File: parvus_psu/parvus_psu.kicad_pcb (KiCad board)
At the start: 2 copper layers, 70 x 100 mm, 30 parts, among them J1 tr_sec, J2 switch, J3 ac_input, J4 tr_pri, J5 left_power, J6 right_power

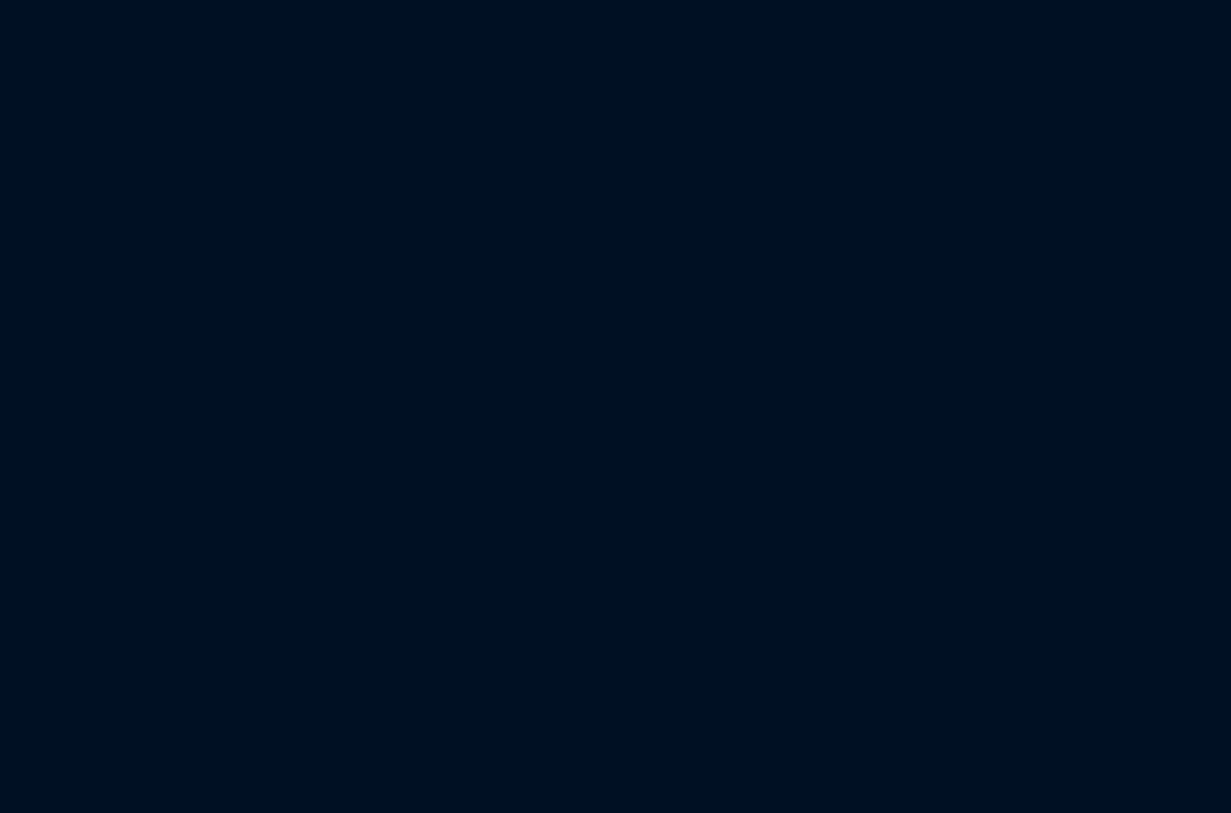
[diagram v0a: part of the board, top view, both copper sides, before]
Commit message: Finished schematic for AC detection circuit and clipping signaling.
Signed-off-by: Nenad Radulovic <nenad.b.radulovic@gmail.com>
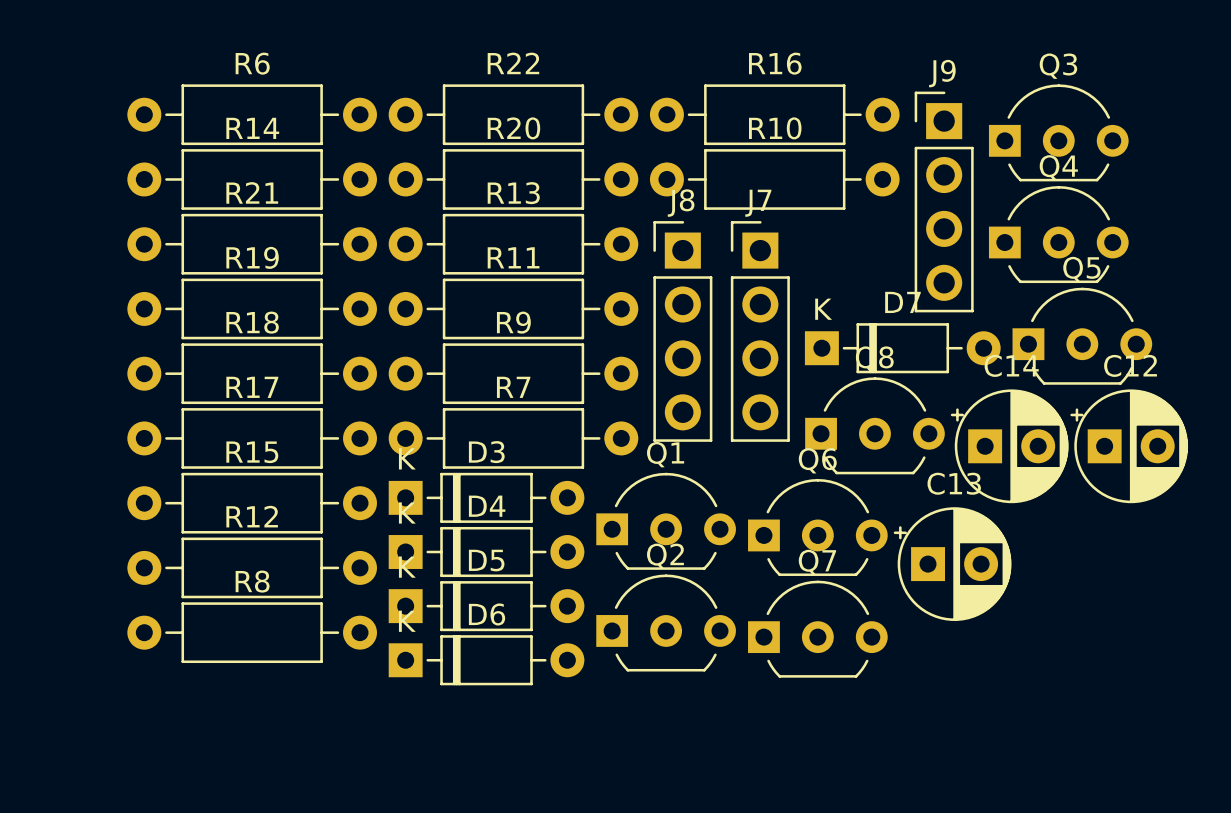
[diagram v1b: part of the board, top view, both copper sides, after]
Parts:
- added C12: 1u, Capacitor_THT:CP_Radial_D5.0mm_P2.50mm, F.Cu at (186.4, 57.1)
- added C13: 1u, Capacitor_THT:CP_Radial_D5.0mm_P2.50mm, F.Cu at (178.0, 62.6)
- added C14: 1u, Capacitor_THT:CP_Radial_D5.0mm_P2.50mm, F.Cu at (180.7, 57.1)
- added D3: 1N4148, Diode_THT:D_DO-35_SOD27_P7.62mm_Horizontal, F.Cu at (153.4, 59.5)
- added D4: 1N4148, Diode_THT:D_DO-35_SOD27_P7.62mm_Horizontal, F.Cu at (153.4, 62.1)
- added D5: 1N4148, Diode_THT:D_DO-35_SOD27_P7.62mm_Horizontal, F.Cu at (153.4, 64.6)
- added D6: 1N4148, Diode_THT:D_DO-35_SOD27_P7.62mm_Horizontal, F.Cu at (153.4, 67.2)
- added D7: 1N4148, Diode_THT:D_DO-35_SOD27_P7.62mm_Horizontal, F.Cu at (173.0, 52.5)
- added J7: signal, Connector_PinHeader_2.54mm:PinHeader_1x04_P2.54mm_Vertical, F.Cu at (170.1, 47.9)
- added J8: ctrl_1, Connector_PinHeader_2.54mm:PinHeader_1x04_P2.54mm_Vertical, F.Cu at (166.5, 47.9)
- added J9: ctrl_2, Connector_PinHeader_2.54mm:PinHeader_1x04_P2.54mm_Vertical, F.Cu at (178.8, 41.8)
- added Q1: BC546B, Package_TO_SOT_THT:TO-92_Inline_Wide, F.Cu at (163.2, 61.0)
- added Q2: BC546B, Package_TO_SOT_THT:TO-92_Inline_Wide, F.Cu at (163.2, 65.8)
- added Q3: BC546B, Package_TO_SOT_THT:TO-92_Inline_Wide, F.Cu at (181.7, 42.7)
- added Q4: BC546B, Package_TO_SOT_THT:TO-92_Inline_Wide, F.Cu at (181.7, 47.5)
- added Q5: BC546B, Package_TO_SOT_THT:TO-92_Inline_Wide, F.Cu at (182.8, 52.3)
- added Q6: BC556B, Package_TO_SOT_THT:TO-92_Inline_Wide, F.Cu at (170.3, 61.3)
- added Q7: BC556B, Package_TO_SOT_THT:TO-92_Inline_Wide, F.Cu at (170.3, 66.1)
- added Q8: BC556B, Package_TO_SOT_THT:TO-92_Inline_Wide, F.Cu at (173.0, 56.5)
- added R10: 100k, Resistor_THT:R_Axial_DIN0207_L6.3mm_D2.5mm_P10.16mm_Horizontal, F.Cu at (165.7, 44.5)
- added R11: 100, Resistor_THT:R_Axial_DIN0207_L6.3mm_D2.5mm_P10.16mm_Horizontal, F.Cu at (153.4, 50.6)
- added R12: 100k, Resistor_THT:R_Axial_DIN0207_L6.3mm_D2.5mm_P10.16mm_Horizontal, F.Cu at (141.1, 62.8)
- added R13: 100, Resistor_THT:R_Axial_DIN0207_L6.3mm_D2.5mm_P10.16mm_Horizontal, F.Cu at (153.4, 47.6)
- added R14: 100k, Resistor_THT:R_Axial_DIN0207_L6.3mm_D2.5mm_P10.16mm_Horizontal, F.Cu at (141.1, 44.5)
- added R15: 100k, Resistor_THT:R_Axial_DIN0207_L6.3mm_D2.5mm_P10.16mm_Horizontal, F.Cu at (141.1, 59.8)
- added R16: 22k, Resistor_THT:R_Axial_DIN0207_L6.3mm_D2.5mm_P10.16mm_Horizontal, F.Cu at (165.7, 41.5)
- added R17: 22k, Resistor_THT:R_Axial_DIN0207_L6.3mm_D2.5mm_P10.16mm_Horizontal, F.Cu at (141.1, 56.7)
- added R18: 22k, Resistor_THT:R_Axial_DIN0207_L6.3mm_D2.5mm_P10.16mm_Horizontal, F.Cu at (141.1, 53.7)
- added R19: 22k, Resistor_THT:R_Axial_DIN0207_L6.3mm_D2.5mm_P10.16mm_Horizontal, F.Cu at (141.1, 50.6)
- added R20: 22k, Resistor_THT:R_Axial_DIN0207_L6.3mm_D2.5mm_P10.16mm_Horizontal, F.Cu at (153.4, 44.5)
- added R21: 10k, Resistor_THT:R_Axial_DIN0207_L6.3mm_D2.5mm_P10.16mm_Horizontal, F.Cu at (141.1, 47.6)
- added R22: 10k, Resistor_THT:R_Axial_DIN0207_L6.3mm_D2.5mm_P10.16mm_Horizontal, F.Cu at (153.4, 41.5)
- added R6: 100k, Resistor_THT:R_Axial_DIN0207_L6.3mm_D2.5mm_P10.16mm_Horizontal, F.Cu at (141.1, 41.5)
- added R7: 10k, Resistor_THT:R_Axial_DIN0207_L6.3mm_D2.5mm_P10.16mm_Horizontal, F.Cu at (153.4, 56.7)
- added R8: 47k, Resistor_THT:R_Axial_DIN0207_L6.3mm_D2.5mm_P10.16mm_Horizontal, F.Cu at (141.1, 65.9)
- added R9: 100k, Resistor_THT:R_Axial_DIN0207_L6.3mm_D2.5mm_P10.16mm_Horizontal, F.Cu at (153.4, 53.7)
- J5: value left_power -> power_1
- J6: value right_power -> power_2
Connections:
- net /acs_n renamed acs_n
- net /acs_p renamed acs_p

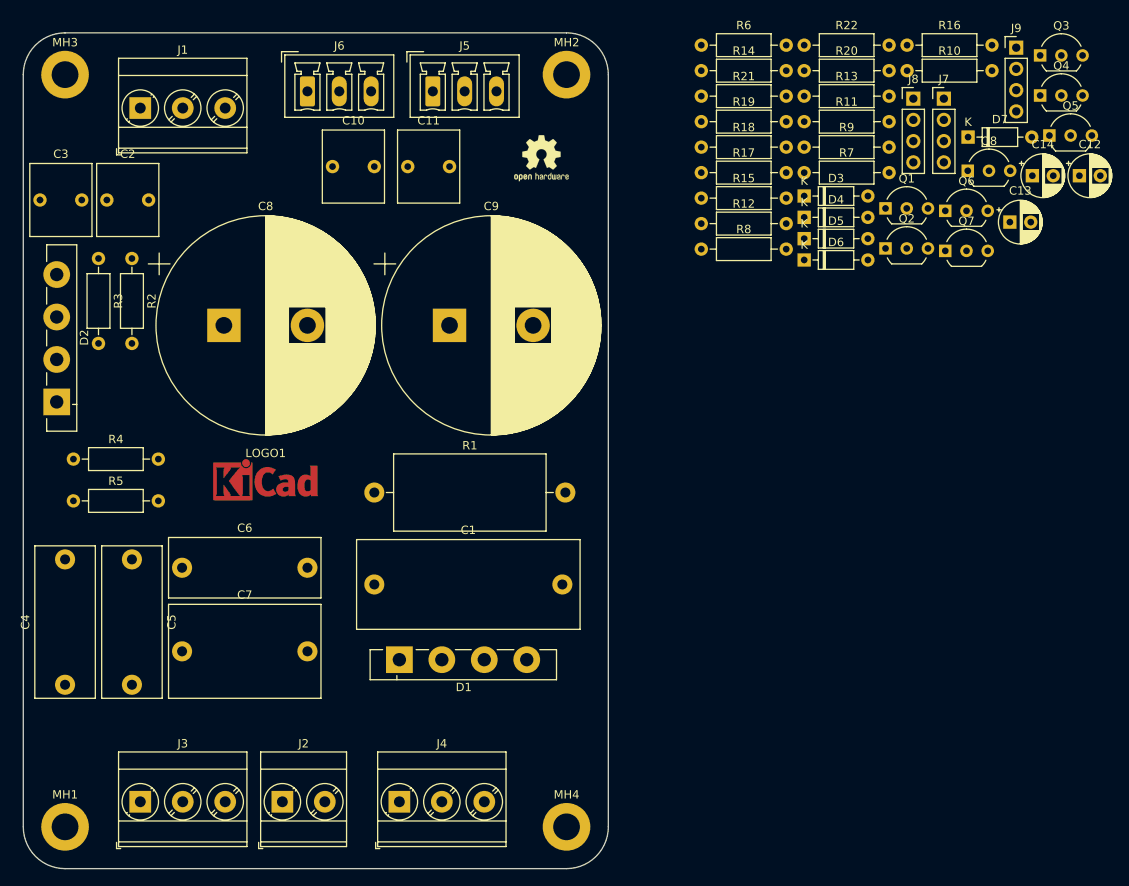
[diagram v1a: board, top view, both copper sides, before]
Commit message: Preliminary placement of AC detect and clipping circuitry.
Signed-off-by: Nenad Radulovic <nenad.b.radulovic@gmail.com>
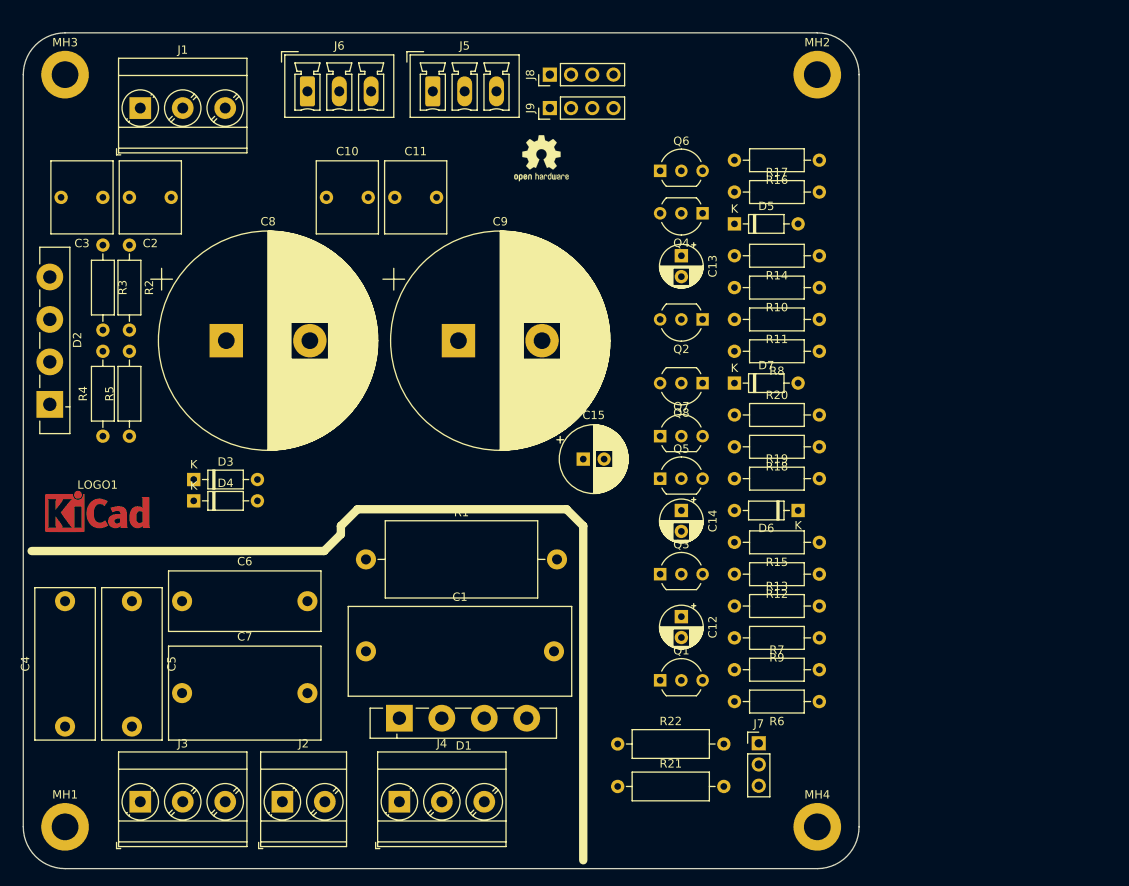
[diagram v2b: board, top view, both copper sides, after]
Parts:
- added C15: 10u, Capacitor_THT:CP_Radial_D8.0mm_P2.50mm, F.Cu at (127.0, 91.0)
- C12, C14: value 1u -> 2u2
- C13: value 1u -> 4u7
- J7: footprint Connector_PinHeader_2.54mm:PinHeader_1x04_P2.54mm_Vertical -> Connector_PinHeader_2.54mm:PinHeader_1x03_P2.54mm_Vertical
- R21, R22: value 10k -> 4k7; footprint Resistor_THT:R_Axial_DIN0207_L6.3mm_D2.5mm_P10.16mm_Horizontal -> Resistor_THT:R_Axial_DIN0309_L9.0mm_D3.2mm_P12.70mm_Horizontal
- moved R22 86.5 mm to (131.1, 125.1)
- moved R21 83.2 mm to (131.1, 130.2)
- moved D3 80.5 mm to (80.4, 93.4)
- moved D4 80.5 mm to (80.4, 96.0)
- moved J7 80.2 mm to (148.0, 125.0)
- moved R6 79.8 mm to (155.2, 120.0), turned to 180 degrees
- moved Q3 76.9 mm to (136.2, 104.8)
- moved C12 71.1 mm to (138.7, 109.8), turned to 270 degrees
- moved Q1 62.6 mm to (136.2, 117.5)
- moved Q5 62.1 mm to (136.2, 93.3)
- moved R13 61.6 mm to (145.1, 108.6)
- moved R7 60.1 mm to (145.1, 116.2)
- moved R9 58.7 mm to (155.2, 112.4), turned to 180 degrees
- moved C14 58.0 mm to (138.7, 97.2), turned to 270 degrees
- moved J9 56.3 mm to (123.0, 49.0), turned to 90 degrees
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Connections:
- Q6 pad 1: Net-(Q4-Pad1) -> Net-(Q6-Pad1)
- Q6 pad 2: Net-(Q6-Pad2) -> Net-(Q4-Pad1)
- Q7 pad 1: Net-(Q5-Pad1) -> Net-(D7-Pad2)
- Q7 pad 2: Net-(D7-Pad2) -> Net-(Q5-Pad1)
- Q8 pad 1: Net-(D7-Pad2) -> GNDPWR
- Q8 pad 2: GNDPWR -> Net-(D7-Pad2)
- R22 pad 1: Net-(Q6-Pad2) -> Net-(J7-Pad1)
- R22 pad 2: Net-(J7-Pad1) -> Net-(Q6-Pad1)
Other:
- board size 70 x 100 mm -> 100 x 100 mm

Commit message: Updated to new version v1.02.
Signed-off-by: Nenad Radulovic <nenad.b.radulovic@gmail.com>
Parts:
- removed D3, D4, D5, D6, D7: 1N4148, Diode_THT:D_DO-35_SOD27_P7.62mm_Horizontal
- removed Q1, Q2, Q3, Q4, Q5: BC546B, Package_TO_SOT_THT:TO-92_Inline_Wide
- removed Q6, Q7, Q8: BC556B, Package_TO_SOT_THT:TO-92_Inline_Wide
- removed R10, R12, R14, R15: 100k, Resistor_THT:R_Axial_DIN0207_L6.3mm_D2.5mm_P10.16mm_Horizontal
- removed R11, R13: 100, Resistor_THT:R_Axial_DIN0207_L6.3mm_D2.5mm_P10.16mm_Horizontal
- removed R16, R17, R18, R19, R20: 22k, Resistor_THT:R_Axial_DIN0207_L6.3mm_D2.5mm_P10.16mm_Horizontal
- removed R21, R22: 4k7, Resistor_THT:R_Axial_DIN0309_L9.0mm_D3.2mm_P12.70mm_Horizontal
- added J10: ctrl_2, Connector_PinHeader_2.54mm:PinHeader_1x04_P2.54mm_Vertical, F.Cu at (123.0, 44.6)
- added J11: signal, Connector_PinHeader_2.54mm:PinHeader_1x03_P2.54mm_Vertical, F.Cu at (155.0, 54.7)
- added U1: L7805, Package_TO_SOT_THT:TO-220-3_Vertical, F.Cu at (135.7, 125.3)
- added U2: PIC18F26K20_ISS, Package_DIP:DIP-28_W7.62mm_LongPads, F.Cu at (140.3, 59.8)
- C12: value 2u2 -> 470n; footprint Capacitor_THT:CP_Radial_D5.0mm_P2.50mm -> Capacitor_THT:C_Rect_L7.2mm_W8.5mm_P5.00mm_FKP2_FKP2_MKS2_MKP2
- C13: value 4u7 -> 10u; footprint Capacitor_THT:CP_Radial_D5.0mm_P2.50mm -> Capacitor_THT:CP_Radial_D8.0mm_P2.50mm
- C14: value 2u2 -> 10u; footprint Capacitor_THT:CP_Radial_D5.0mm_P2.50mm -> Capacitor_THT:CP_Radial_D8.0mm_P2.50mm
- C15: value 10u -> 470n; footprint Capacitor_THT:CP_Radial_D8.0mm_P2.50mm -> Capacitor_THT:C_Rect_L7.2mm_W8.5mm_P5.00mm_FKP2_FKP2_MKS2_MKP2
- J8: value ctrl_1 -> prog
- J9: value ctrl_2 -> ctrl_1
- R7: value 10k -> 100k
- R8: value 47k -> 1k; footprint Resistor_THT:R_Axial_DIN0207_L6.3mm_D2.5mm_P10.16mm_Horizontal -> Resistor_THT:R_Axial_DIN0309_L9.0mm_D3.2mm_P12.70mm_Horizontal
- R9: value 100k -> 1k; footprint Resistor_THT:R_Axial_DIN0207_L6.3mm_D2.5mm_P10.16mm_Horizontal -> Resistor_THT:R_Axial_DIN0309_L9.0mm_D3.2mm_P12.70mm_Horizontal
- moved C13 46.5 mm to (137.2, 113.2)
- moved J8 38.5 mm to (155.0, 66.4), turned to 0 degrees
- moved C14 35.3 mm to (138.2, 132.5)
- moved R8 26.9 mm to (156.0, 105.0)
- moved C12 10.0 mm to (137.2, 99.9)
- moved R9 3.31 mm to (155.5, 109.1)
- moved R7 2.54 mm to (145.1, 113.7)
- moved J7 0.96 mm to (148.9, 125.3), turned to 90 degrees
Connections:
- C13 pad 1: Net-(C13-Pad1) -> /vcc
- C14 pad 1: Net-(C14-Pad1) -> vdd
- C15 pad 1: /vcc -> vdd
- J8 pad 1: (no net) -> vdd
- J8 pad 2: /mute_control -> Net-(J8-Pad2)
- J8 pad 4: /clipping -> Net-(J8-Pad4)
- R6 pad 1: Net-(D3-Pad1) -> acs_p
- R6 pad 2: Net-(Q1-Pad2) -> /ac_detect
- R7 pad 1: Net-(Q1-Pad2) -> vdd
- R7 pad 2: GNDPWR -> Net-(J8-Pad2)
- R8 pad 1: /vcc -> Net-(J7-Pad3)
- R8 pad 2: /clipping -> Net-(R8-Pad2)
- R9 pad 1: /vcc -> Net-(J7-Pad1)
- R9 pad 2: /ac_detect -> Net-(R9-Pad2)

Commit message: Project update
Signed-off-by: Nenad Radulovic <nenad.b.radulovic@gmail.com>
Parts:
- removed J10: ctrl_2, Connector_PinHeader_2.54mm:PinHeader_1x04_P2.54mm_Vertical
- removed J11: signal, Connector_PinHeader_2.54mm:PinHeader_1x03_P2.54mm_Vertical
- removed U1: L7805, Package_TO_SOT_THT:TO-220-3_Vertical
- removed U2: PIC18F26K20_ISS, Package_DIP:DIP-28_W7.62mm_LongPads
- added D3: 1N4148, Diode_THT:D_DO-35_SOD27_P7.62mm_Horizontal, F.Cu at (80.4, 93.4)
- added D4: 1N4148, Diode_THT:D_DO-35_SOD27_P7.62mm_Horizontal, F.Cu at (80.4, 96.0)
- added D5: 1N4148, Diode_THT:D_DO-35_SOD27_P7.62mm_Horizontal, F.Cu at (145.1, 62.9)
- added D6: 1N4148, Diode_THT:D_DO-35_SOD27_P7.62mm_Horizontal, F.Cu at (152.7, 97.2)
- added D7: 1N4148, Diode_THT:D_DO-35_SOD27_P7.62mm_Horizontal, F.Cu at (145.1, 81.9)
- added Q1: BC546B, Package_TO_SOT_THT:TO-92_Inline_Wide, F.Cu at (136.2, 117.5)
- added Q2: BC546B, Package_TO_SOT_THT:TO-92_Inline_Wide, F.Cu at (141.3, 74.3)
- added Q3: BC546B, Package_TO_SOT_THT:TO-92_Inline_Wide, F.Cu at (136.2, 104.8)
- added Q4: BC546B, Package_TO_SOT_THT:TO-92_Inline_Wide, F.Cu at (141.3, 61.6)
- added Q5: BC546B, Package_TO_SOT_THT:TO-92_Inline_Wide, F.Cu at (136.2, 93.3)
- added Q6: BC556B, Package_TO_SOT_THT:TO-92_Inline_Wide, F.Cu at (136.2, 56.5)
- added Q7: BC556B, Package_TO_SOT_THT:TO-92_Inline_Wide, F.Cu at (136.2, 88.3)
- added Q8: BC556B, Package_TO_SOT_THT:TO-92_Inline_Wide, F.Cu at (141.3, 81.9)
- added R10: 100k, Resistor_THT:R_Axial_DIN0207_L6.3mm_D2.5mm_P10.16mm_Horizontal, F.Cu at (155.2, 70.5)
- added R11: 100, Resistor_THT:R_Axial_DIN0207_L6.3mm_D2.5mm_P10.16mm_Horizontal, F.Cu at (155.2, 74.3)
- added R12: 100k, Resistor_THT:R_Axial_DIN0207_L6.3mm_D2.5mm_P10.16mm_Horizontal, F.Cu at (155.2, 104.8)
- added R13: 100, Resistor_THT:R_Axial_DIN0207_L6.3mm_D2.5mm_P10.16mm_Horizontal, F.Cu at (145.1, 108.6)
- added R14: 100k, Resistor_THT:R_Axial_DIN0207_L6.3mm_D2.5mm_P10.16mm_Horizontal, F.Cu at (155.2, 66.7)
- added R15: 100k, Resistor_THT:R_Axial_DIN0207_L6.3mm_D2.5mm_P10.16mm_Horizontal, F.Cu at (155.2, 101.0)
- added R16: 22k, Resistor_THT:R_Axial_DIN0207_L6.3mm_D2.5mm_P10.16mm_Horizontal, F.Cu at (155.2, 55.2)
- added R17: 22k, Resistor_THT:R_Axial_DIN0207_L6.3mm_D2.5mm_P10.16mm_Horizontal, F.Cu at (145.1, 59.0)
- added R18: 22k, Resistor_THT:R_Axial_DIN0207_L6.3mm_D2.5mm_P10.16mm_Horizontal, F.Cu at (155.2, 89.5)
- added R19: 22k, Resistor_THT:R_Axial_DIN0207_L6.3mm_D2.5mm_P10.16mm_Horizontal, F.Cu at (145.1, 93.3)
- added R20: 22k, Resistor_THT:R_Axial_DIN0207_L6.3mm_D2.5mm_P10.16mm_Horizontal, F.Cu at (145.1, 85.7)
- added R21: 4k7, Resistor_THT:R_Axial_DIN0309_L9.0mm_D3.2mm_P12.70mm_Horizontal, F.Cu at (131.1, 130.2)
- added R22: 4k7, Resistor_THT:R_Axial_DIN0309_L9.0mm_D3.2mm_P12.70mm_Horizontal, F.Cu at (131.1, 125.1)
- C12: value 470n -> 2u2; footprint Capacitor_THT:C_Rect_L7.2mm_W8.5mm_P5.00mm_FKP2_FKP2_MKS2_MKP2 -> Capacitor_THT:CP_Radial_D5.0mm_P2.50mm
- C13: value 10u -> 4u7; footprint Capacitor_THT:CP_Radial_D8.0mm_P2.50mm -> Capacitor_THT:CP_Radial_D5.0mm_P2.50mm
- C14: value 10u -> 2u2; footprint Capacitor_THT:CP_Radial_D8.0mm_P2.50mm -> Capacitor_THT:CP_Radial_D5.0mm_P2.50mm
- C15: value 470n -> 10u; footprint Capacitor_THT:C_Rect_L7.2mm_W8.5mm_P5.00mm_FKP2_FKP2_MKS2_MKP2 -> Capacitor_THT:CP_Radial_D8.0mm_P2.50mm
- J8: value prog -> ctrl_1
- J9: value ctrl_1 -> ctrl_2
- R7: value 100k -> 10k
- R8: value 1k -> 47k; footprint Resistor_THT:R_Axial_DIN0309_L9.0mm_D3.2mm_P12.70mm_Horizontal -> Resistor_THT:R_Axial_DIN0207_L6.3mm_D2.5mm_P10.16mm_Horizontal
- R9: value 1k -> 100k; footprint Resistor_THT:R_Axial_DIN0309_L9.0mm_D3.2mm_P12.70mm_Horizontal -> Resistor_THT:R_Axial_DIN0207_L6.3mm_D2.5mm_P10.16mm_Horizontal
- moved C13 46.5 mm to (138.7, 66.7)
- moved J8 38.5 mm to (123.0, 45.0), turned to 90 degrees
- moved C14 35.3 mm to (138.7, 97.2)
- moved R8 26.9 mm to (155.2, 78.1)
- moved C12 10.0 mm to (138.7, 109.8)
- moved R9 3.31 mm to (155.2, 112.4)
- moved R7 2.54 mm to (145.1, 116.2)
- moved J7 0.96 mm to (148.0, 125.0), turned to 0 degrees
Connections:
- C13 pad 1: /vcc -> Net-(C13-Pad1)
- C14 pad 1: vdd -> Net-(C14-Pad1)
- C15 pad 1: vdd -> /vcc
- J8 pad 1: vdd -> (no net)
- J8 pad 2: Net-(J8-Pad2) -> /mute_control
- J8 pad 4: Net-(J8-Pad4) -> /clipping
- R6 pad 1: acs_p -> Net-(D3-Pad1)
- R6 pad 2: /ac_detect -> Net-(Q1-Pad2)
- R7 pad 1: vdd -> Net-(Q1-Pad2)
- R7 pad 2: Net-(J8-Pad2) -> GNDPWR
- R8 pad 1: Net-(J7-Pad3) -> /vcc
- R8 pad 2: Net-(R8-Pad2) -> /clipping
- R9 pad 1: Net-(J7-Pad1) -> /vcc
- R9 pad 2: Net-(R9-Pad2) -> /ac_detect
